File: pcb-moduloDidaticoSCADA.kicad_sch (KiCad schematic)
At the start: 17 parts, among them J1 alimentação 12 Vcc, J2 RS485, J3 DS18B20, U1 NODEMCU

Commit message: readme atualizado
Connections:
- net PWM_LAMP/D1/IO5 renamed PWM_RESISTENCIA/D1/IO5
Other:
- moved on the sheet: RV1, U1

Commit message: organização e legendas do esquemático
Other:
- note added: "MÓDULO MICROCONTROLADOR NODEMCU - ESP8266"
- note added: "RS485"
- note added: "SAÍDAS DISCRETAS E PWM"
- note added: "SENSOR DE TEMPERATURA"
- note added: "SINAL ANALÓFICO"
- note removed: "SAÍDAS DISCRETAS"
- moved on the sheet: C1, C6, C7, C8, H1, H2, H3, H4, J2, J3, R1, R2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

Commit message: style: ajustes no layout
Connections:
- net 3V3: now also RV1.3
- net EA1/A0/ADC: no longer RV1.3
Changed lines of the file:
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@@
-		)
-	)
-	(label "EA1{slash}A0{slash}ADC"
-		(at 260.096 61.722 180)
-		(effects
-			(font
-				(size 1.27 1.27)
-			)
-			(justify right bottom)
 		)
 	)
@@
 		(effects
 			(font
+				(size 1.27 1.27)
+			)
+			(justify right bottom)
+		)
+	)
+	(label "3V3"
+		(at 260.096 61.722 180)
+		(effects
+			(font

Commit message: ajustes no layout e serigrafia
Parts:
- added H5, H6, H7, H8: MountingHole, MountingHole:MountingHole_3.2mm_M3, symbol Mechanical:MountingHole
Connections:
- net 3.3V is gone; now on net 3V3: J3.3 (Pin_3), R4.1, U1.16 (3.3V)
- net +5V: no longer C8.2
- net 3V3: now also C8.2
- net RST: no longer names the net of U1.1 (RST)
- net RST: no longer U1.13 (RST)
- no-connect marks 8 -> 10
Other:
- sheet alimentação ports: added 5V_SERVO; removed none
- sheet saídas ports: added 5V_IN_SERVO; removed none
- note added: "SAÍDAS DISCRETAS Tipo Base 1 Base 0 Função Pino GPIO Coil 00001 0 Saída discreta 1 D0 GPIO16 Coil 00002 1 Saída discreta 2 TX GPIO1 ENTRADAS DISCRETAS Tipo Base 1 Base 0 Função Pino GPIO Discrete Input 10001 0 Entrada discreta 1 D8 GPIO15 Discrete Input 10002 1 Entrada discreta 2 RX GPIO3 ENTRADAS ANALÓGICAS/NUMÉRICAS Tipo Base 1 Base 0 Função Pino Faixa Input Register 30001 0 ADC A0 0..1023 Inpu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"
- note removed: "SAÍDAS DISCRETAS Tipo Base 1 Base 0 Função Pino GPIO Coil 00001 0 Saída discreta 1 D0 GPIO16 Coil 00002 1 Saída discreta 2 TX GPIO1 Coil 00003 2 Saída discreta 3 SD3 GPIO10 ENTRADAS DISCRETAS Tipo Base 1 Base 0 Função Pino GPIO Discrete Input 10001 0 Entrada discreta 1 D8 GPIO15 Discrete Input 10002 1 Entrada discreta 2 RX GPIO3 ENTRADAS ANALÓGICAS/NUMÉRICAS Tipo Base 1 Base 0 Função Pino Faixa I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"

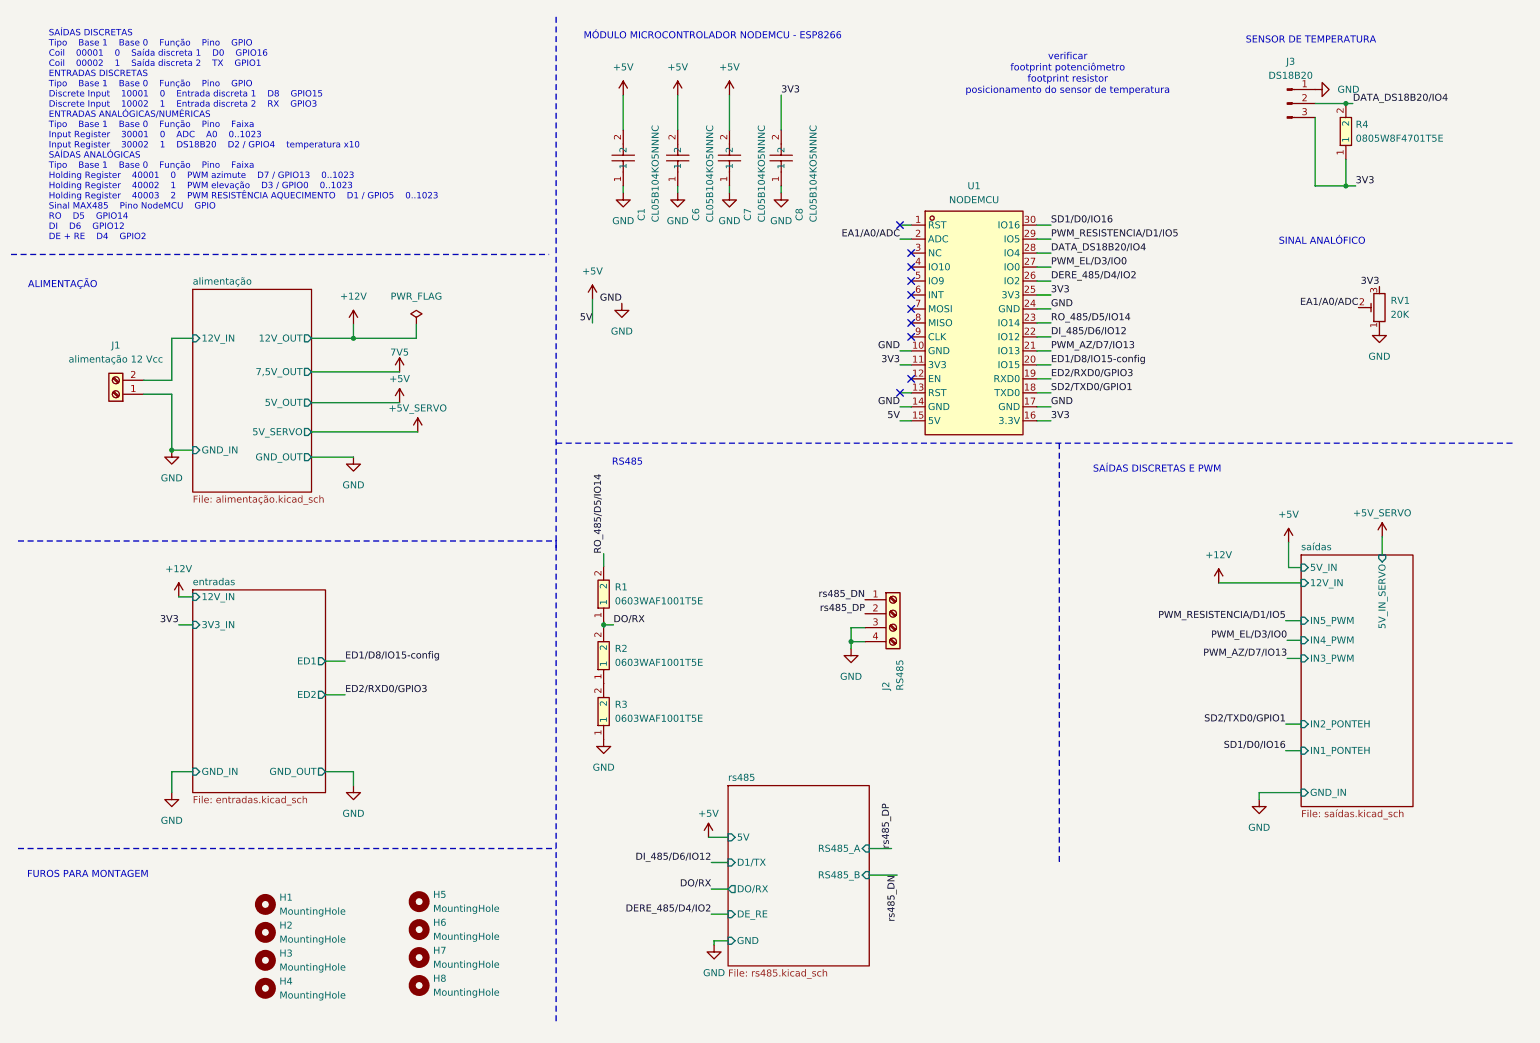
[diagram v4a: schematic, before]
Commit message: ajusta circuitos de entrada, alimentação e saída e adiciona visualizações da PCB
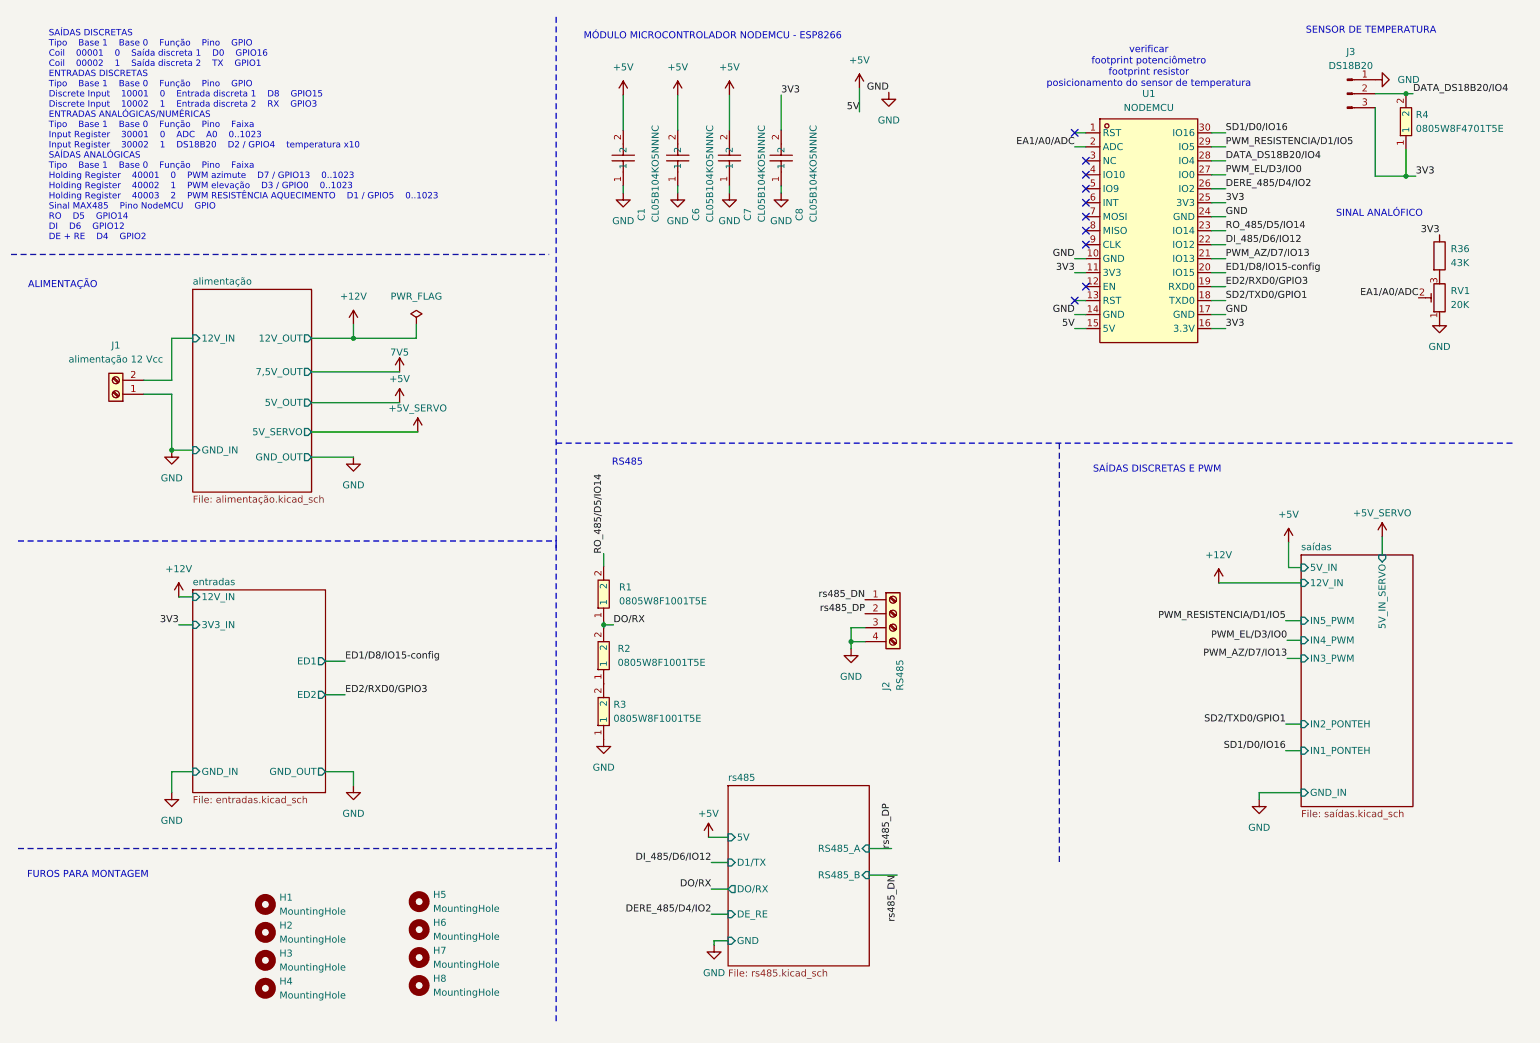
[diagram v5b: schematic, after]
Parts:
- removed R1, R2, R3: 0603WAF1001T5E, jlclib:R0603, symbol a_jlclib:0603WAF1001T5E
- added R1, R2, R3: 0805W8F1001T5E, jlclib:R0805, symbol a_jlclib:0805W8F1001T5E
- added R36: 43K, Resistor_SMD:R_0805_2012Metric_Pad1.20x1.40mm_HandSolder, symbol Device:R
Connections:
- net 3V3: now also R36.1; no longer RV1.3
- net DO/RX: now also R1.1, R2.2
- net GND: now also R3.1
- net RO_485/D5/IO14: now also R1.2
- new net: R2.1, R3.2
- new net: R36.2, RV1.3
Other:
- moved on the sheet: J3, R4, RV1, U1
